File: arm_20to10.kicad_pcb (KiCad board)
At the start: 2 copper layers, 12.2 x 28.4 mm, 10 parts, among them J1 ARM_20PIN, J2 ARM_10PIN, SW1 DUAL_SWITCH_INV, U1 AAT3221 or LP5907

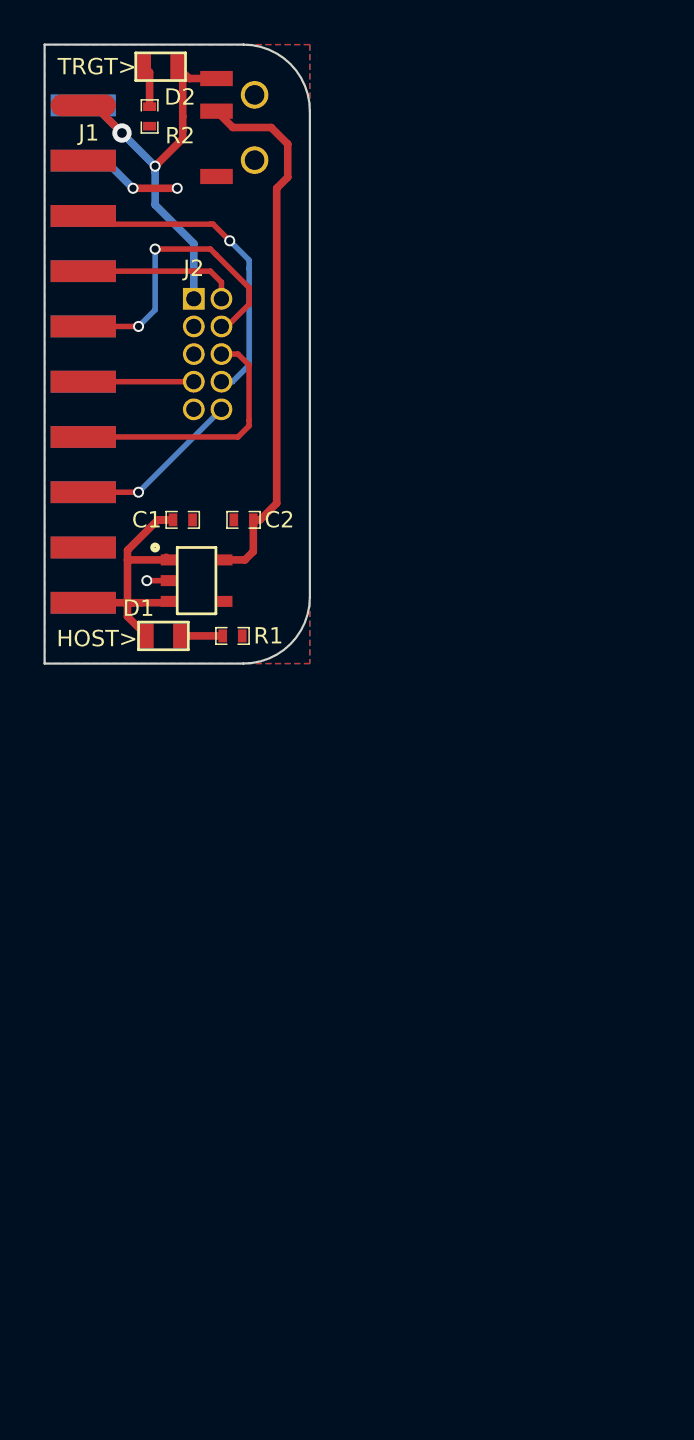
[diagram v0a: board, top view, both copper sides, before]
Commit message: - start reworking board with new 20 pin header
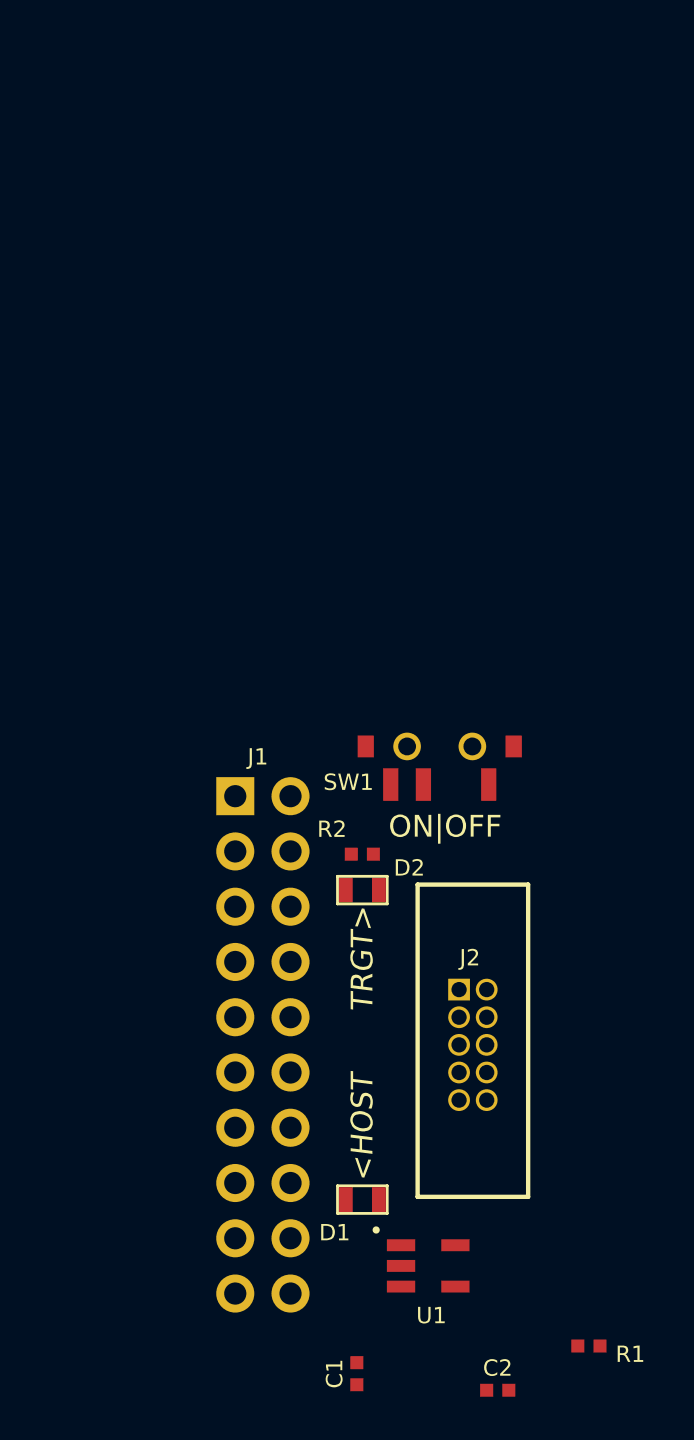
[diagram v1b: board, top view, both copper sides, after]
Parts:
- C1, C2, R1, R2: footprint SM0402 -> SM0402_np
- J1: footprint ARM_20PIN_EDGE_BOTH -> ARM_20_PIN_TH_RIGHTANGLE
- U1: footprint SOT23-5 -> sot23-5_noah
- moved C2 41.7 mm to (212.1, 182.2), turned to 0 degrees
- moved C1 40.1 mm to (205.6, 181.5), turned to 90 degrees
- moved D2 39.0 mm to (205.9, 159.3)
- moved R1 36.5 mm to (216.3, 180.2), turned to 0 degrees
- moved R2 35.3 mm to (205.9, 157.6), turned to 180 degrees
- moved J2 34.0 mm to (210.3, 166.4)
- moved U1 32.9 mm to (207.6, 176.5), turned to 0 degrees
- moved SW1 29.7 mm to (209.4, 152.7), turned to 180 degrees
- moved J1 27.6 mm to (200.0, 154.9)
- moved D1 27.5 mm to (205.9, 173.5)
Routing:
- net N-000005: track 25.0 -> 0.00 mm
- net /VCC: track 20.8 -> 0.00 mm, vias 2 -> 0
- net /TDI: track 14.9 -> 0.00 mm, vias 1 -> 0
- net /TCLK/SWCLK: track 13.9 -> 0.00 mm, vias 2 -> 0
- net /5V: track 13.2 -> 0.00 mm
- net /SWO/TDO: track 12.1 -> 0.00 mm
- net /NRST: track 7.93 -> 0.00 mm, vias 1 -> 0
- net /TMS/SWDIO: track 7.32 -> 0.00 mm
- net GND: track 5.86 -> 0.00 mm, vias 3 -> 0
- net /RTCK: track 5.08 -> 0.00 mm
- net N-0000011: track 1.96 -> 0.00 mm
- net N-000003: track 1.94 -> 0.00 mm
- removed copper zone on B.Cu, net GND
- removed copper zone on F.Cu, net GND
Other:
- board outline removed
- board text added: "<HOST"
- board text added: "ON|OFF"
- board text removed: "HOST>"
- board text removed: "arm20to10 v0.4 git.io/7mbuGg"

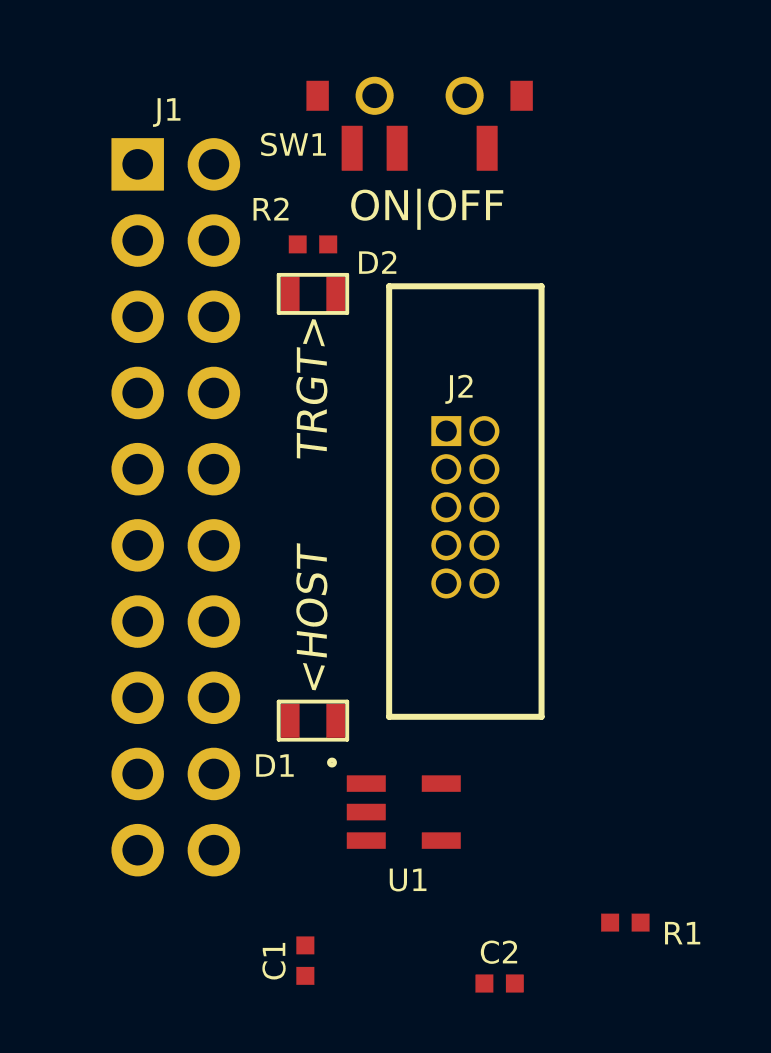
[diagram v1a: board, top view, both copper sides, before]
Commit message: - outline and pours done
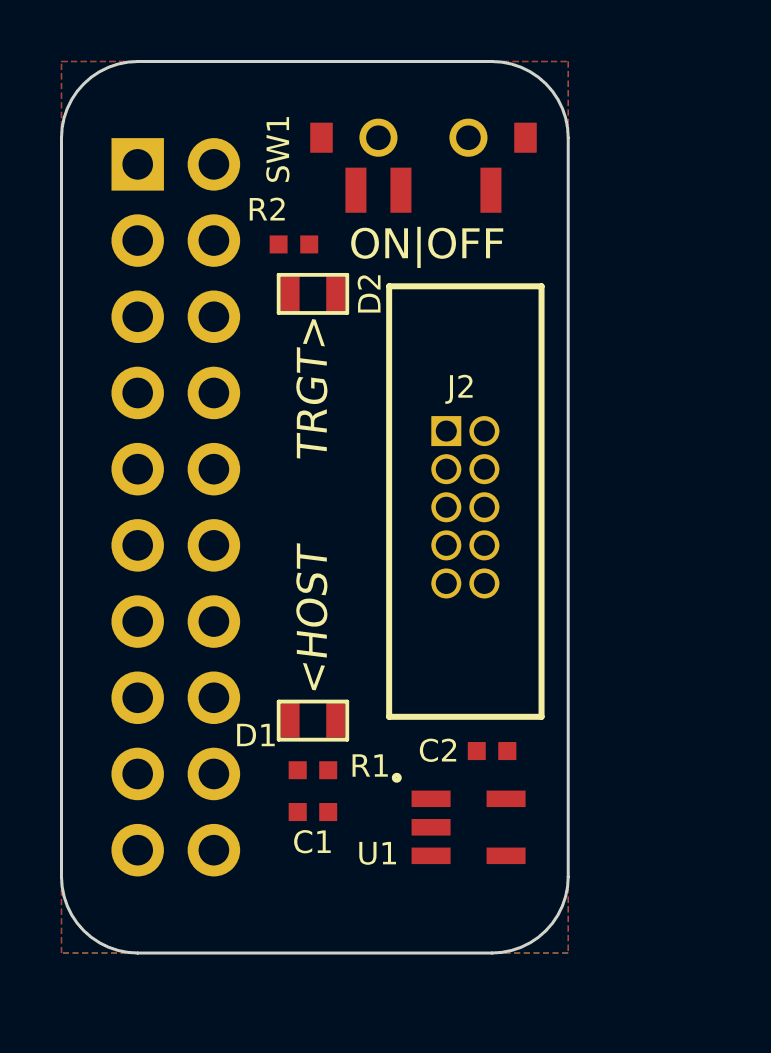
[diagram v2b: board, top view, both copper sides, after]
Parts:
- moved R1 11.6 mm to (205.9, 175.1)
- moved C2 7.75 mm to (211.8, 174.5), turned to 180 degrees
- moved C1 4.96 mm to (205.9, 176.5), turned to 180 degrees
- moved U1 2.22 mm to (209.8, 177.0)
- moved SW1 1.40 mm to (209.6, 154.1)
- moved R2 0.63 mm to (205.2, 157.6)
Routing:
- added copper zone on B.Cu, net GND
- added copper zone on F.Cu, net GND
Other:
- board outline added: 16.9 x 29.7 mm

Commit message: - pcb done.
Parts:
- C1, C2: footprint SM0402_np -> SMD_Packages:SMD-0603_c
- D1, D2: footprint SM0603 -> SMD_Packages:SMD-0603
- J1: value ARM_20PIN -> SFH11-PBPC-D10-RA-BK; footprint ARM_20_PIN_TH_RIGHTANGLE -> kicadlib:ARM_20_PIN_TH_RIGHTANGLE
- J2: value ARM_10PIN -> 20021111-00010T4LF; footprint ARM_10_PIN -> kicadlib:ARM_10_PIN
- R1, R2: footprint SM0402_np -> SMD_Packages:SMD-0603_r
- SW1: value DUAL_SWITCH_INV -> SSSS810701; footprint SWITCH_SLIDE_SSSS810701 -> kicadlib:SWITCH_SLIDE_SSSS810701
- U1: value AAT3221 or LP5907 -> MIC5504-3.3YM5 TR; footprint sot23-5_noah -> kicadlib:sot23-5_noah
- moved C1 2.03 mm to (205.9, 178.6)
- moved U1 0.97 mm to (209.4, 177.9)
- moved R2 0.90 mm to (205.1, 156.7), turned to 270 degrees
- moved C2 0.52 mm to (211.7, 175.0)
- moved R1 0.38 mm to (205.9, 175.5), turned to 180 degrees
- turned D1 to 180 degrees
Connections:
- J1 pad 17: (no net) -> Net-(J1-Pad17)
- J1 pad 3: (no net) -> /TRST
- SW1 pad 1: (no net) -> Net-(SW1-Pad1)
- U1 pad 4: (no net) -> Net-(U1-Pad4)
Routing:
- net /TDI: track 0.00 -> 25.6 mm
- net Net-(C2-Pad1): track 0.00 -> 23.7 mm
- net /VCC: track 0.00 -> 19.8 mm, vias 0 -> 1
- net /5V: track 0.00 -> 19.8 mm
- net /SWO/TDO: track 0.00 -> 18.5 mm
- net /TCLK/SWCLK: track 0.00 -> 18.2 mm
- net /TMS/SWDIO: track 0.00 -> 14.9 mm, vias 0 -> 1
- net /NRST: track 0.00 -> 14.9 mm, vias 0 -> 1
- net /RTCK: track 0.00 -> 11.3 mm
- net Net-(D1-Pad2): track 0.00 -> 2.03 mm
- net Net-(D2-Pad2): track 0.00 -> 1.78 mm
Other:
- rule trace_min: 0.254 -> 0.1524
